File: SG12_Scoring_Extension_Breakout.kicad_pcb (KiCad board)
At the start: 2 copper layers, 100 x 100 mm, 41 parts, among them J1 RJ45, J10 Conn_01x02, J11 Conn_01x02, J12 Conn_01x02, J13 Conn_01x02, J14 Conn_01x02, J15 Conn_01x02, J16 Conn_02x04_Top_Bottom, J17 Conn_02x04_Top_Bottom, J18 Conn_02x04_Top_Bottom, J19 Conn_01x02, J2 Barrel_Jack_MountingPin, J3 Barrel_Jack_MountingPin, J4 Barrel_Jack_MountingPin, J5 Barrel_Jack_MountingPin, J6 Barrel_Jack_MountingPin, J7 Barrel_Jack_MountingPin, J8 Conn_02x08_Odd_Even, J9 Barrel_Jack_MountingPin, Q1 IRF4905, Q2 IRF4905, Q3 IRF4905, Q4 IRF4905, Q5 IRF4905, Q6 IRF4905

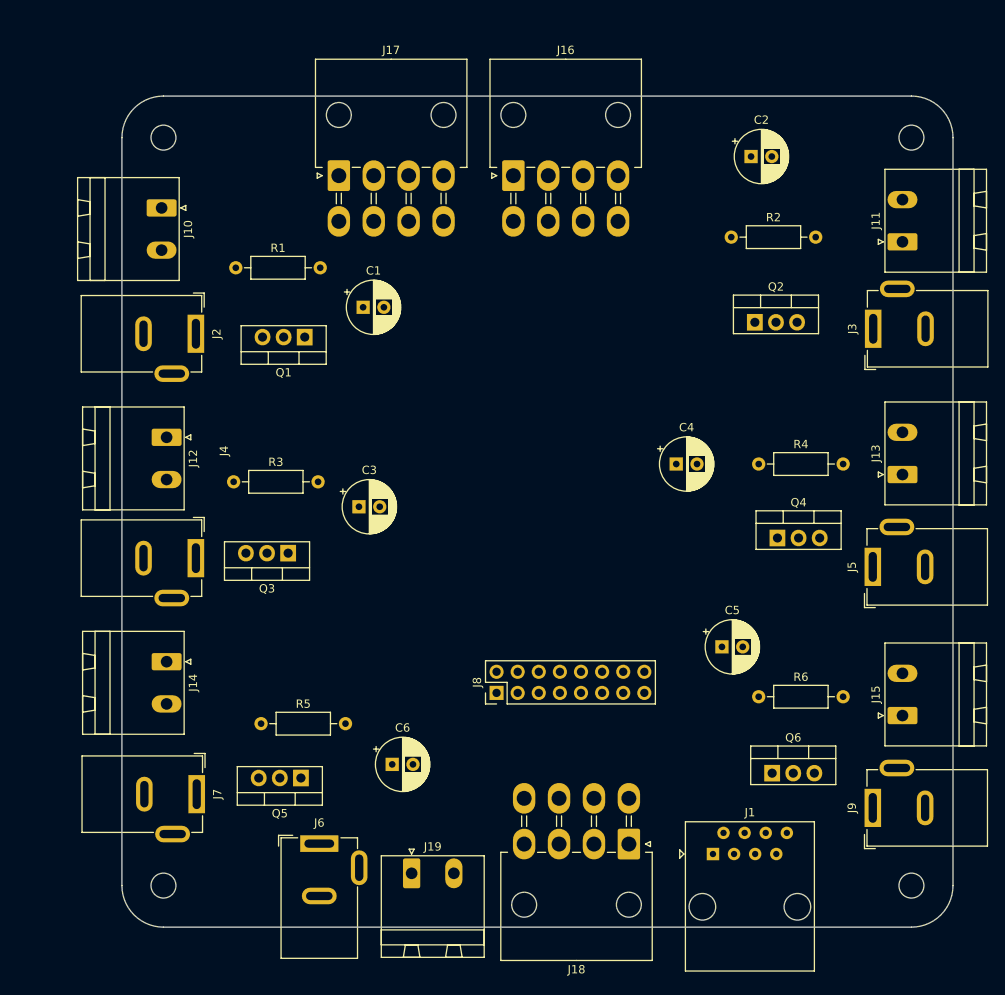
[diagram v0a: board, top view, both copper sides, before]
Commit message: Very nitpicky positioning on the Red and Green connectors
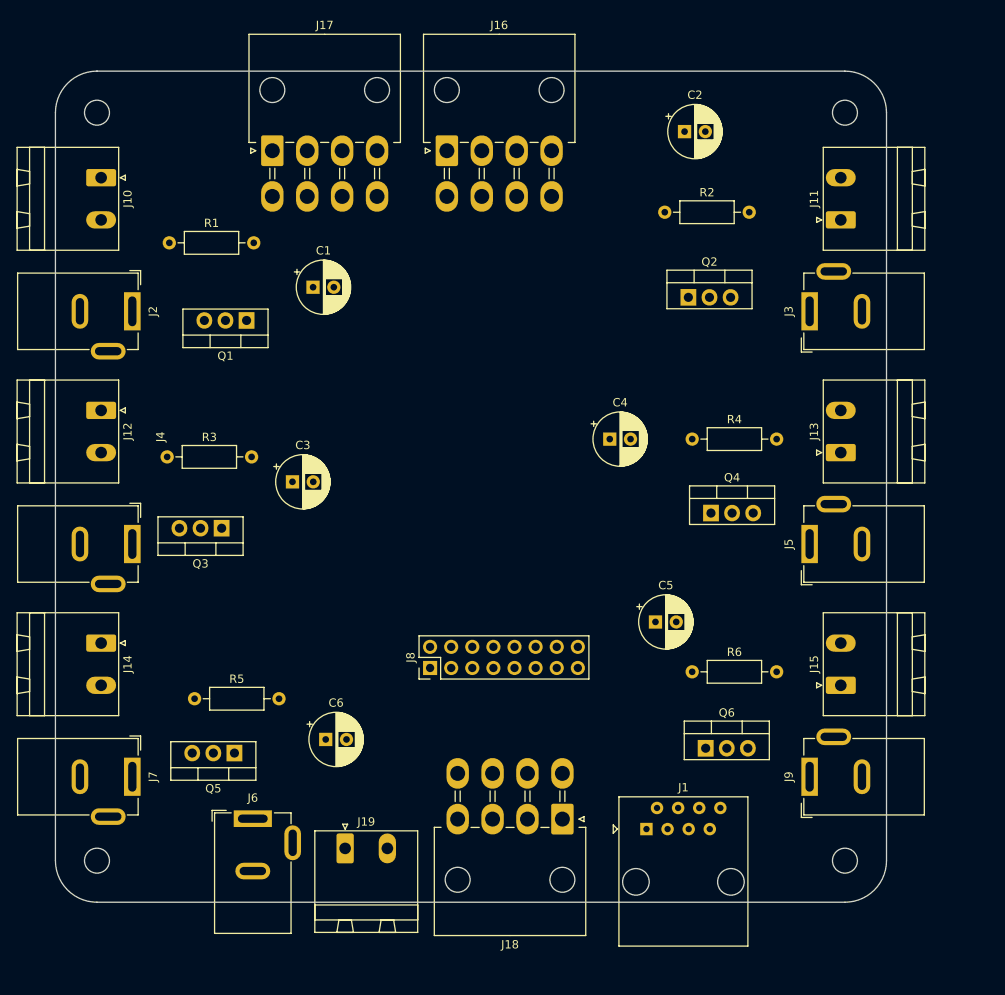
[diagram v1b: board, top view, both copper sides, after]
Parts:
- moved C3 8.54 mm to (123.5, 94.4)
- moved C6 8.54 mm to (127.5, 125.4)
- moved C2 8.54 mm to (170.7, 52.3)
- moved C4 8.54 mm to (161.7, 89.3)
- moved C5 8.54 mm to (167.2, 111.3)
- moved J1 8.54 mm to (166.1, 136.2)
- moved J16 8.54 mm to (142.1, 54.6)
- moved J17 8.54 mm to (121.1, 54.6)
- moved J18 8.54 mm to (156.0, 135.0)
- moved J19 8.54 mm to (129.9, 138.5)
- moved J6 8.54 mm to (118.8, 134.9)
- moved J8 8.54 mm to (140.1, 116.8)
- moved Q2 8.54 mm to (171.2, 72.2)
- moved Q3 8.54 mm to (115.0, 100.0)
- moved Q4 8.54 mm to (173.9, 98.2)
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
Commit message: Very nitpicky mofet and resistor placement
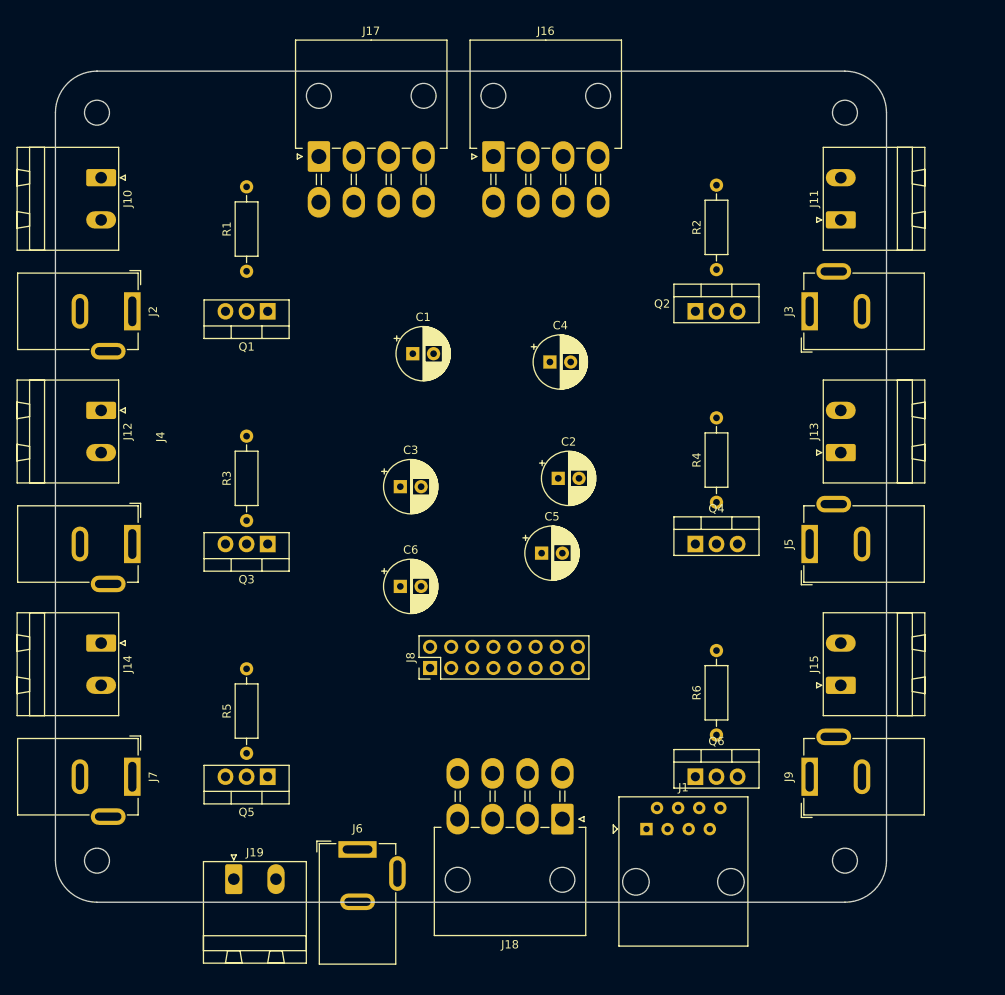
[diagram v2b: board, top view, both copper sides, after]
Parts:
- moved C2 44.4 mm to (155.5, 94.0)
- moved C6 20.5 mm to (136.5, 107.0)
- moved C5 16.0 mm to (153.5, 103.0)
- moved C1 14.4 mm to (138.0, 79.0)
- moved J19 13.9 mm to (116.5, 142.2)
- moved J6 13.1 mm to (131.3, 138.7)
- moved C3 13.0 mm to (136.5, 95.0)
- moved R3 12.3 mm to (118.0, 99.1), turned to 90 degrees
- moved C4 11.7 mm to (154.5, 80.0)
- moved R1 9.91 mm to (118.0, 69.1), turned to 90 degrees
- moved R2 9.29 mm to (174.5, 68.9), turned to 90 degrees
- moved R5 9.07 mm to (118.0, 127.1), turned to 90 degrees
- moved R4 8.15 mm to (174.5, 96.9), turned to 90 degrees
- moved R6 8.15 mm to (174.5, 124.9), turned to 90 degrees
- moved Q3 5.86 mm to (120.5, 101.9)
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
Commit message: Initial footprint placement
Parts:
- moved C6 44.8 mm to (179.5, 119.8), turned to 90 degrees
- moved C5 44.7 mm to (112.0, 119.6), turned to 90 degrees
- moved C2 38.6 mm to (179.5, 63.8), turned to 90 degrees
- moved C1 30.2 mm to (112.0, 63.6), turned to 90 degrees
- moved C4 27.6 mm to (179.5, 91.8), turned to 90 degrees
- moved C3 24.7 mm to (112.0, 91.6), turned to 90 degrees
- moved R3 4.92 mm to (118.0, 94.2)
- moved R5 4.92 mm to (118.0, 122.2)
- moved J19 4.24 mm to (113.5, 139.2)
- moved J8 4.01 mm to (136.5, 118.5)
- moved Q2 3.13 mm to (170.5, 71.2)
- moved Q4 3.13 mm to (170.5, 99.2)
- moved Q6 3.13 mm to (170.5, 127.2)
- moved R2 3.13 mm to (173.0, 66.2)
- moved R4 3.13 mm to (173.0, 94.2)
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
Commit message: Some initial routing
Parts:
- moved J8 7.27 mm to (136.1, 111.3)
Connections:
- J16 pad 6: /Red_PullUp -> /WhiteG_PullUp
- J16 pad 7: /WhiteG_PullUp -> /WhiteR_PullUp
- J16 pad 8: /WhiteR_PullUp -> /Red_PullUp
- J17 pad 6: /Red_PullUp -> /WhiteG_PullUp
- J17 pad 7: /WhiteG_PullUp -> /WhiteR_PullUp
- J17 pad 8: /WhiteR_PullUp -> /Red_PullUp
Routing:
- net /WhiteG_PullUp: track 0.00 -> 153.0 mm, vias 0 -> 1
- net /BlockingG_PullDown: track 0.00 -> 152.2 mm
- net /Green_PullDown: track 0.00 -> 135.4 mm, vias 0 -> 1
- net /WhiteR_PullUp: track 0.00 -> 134.4 mm, vias 0 -> 3
- net /Green_PullUp: track 0.00 -> 128.3 mm
- net /WhiteG_PullDown: track 0.00 -> 127.8 mm, vias 0 -> 1
- net /Red_PullUp: track 0.00 -> 124.7 mm, vias 0 -> 2
- net /Red_PullDown: track 0.00 -> 116.1 mm, vias 0 -> 1
- net /WhiteR_PullDown: track 0.00 -> 84.8 mm, vias 0 -> 1
- net /BlockingG_PullUp: track 0.00 -> 60.0 mm, vias 0 -> 1
- net /BlockingR_PullDown: track 0.00 -> 54.5 mm
- net /BlockingR_PullUp: track 0.00 -> 53.0 mm
- added copper zone on F.Cu, net /BlockingG_PullUp
- added copper zone on F.Cu, net /BlockingR_PullUp
- added copper zone on F.Cu, net /Green_PullUp
- added copper zone on F.Cu, net /Red_PullUp
- added copper zone on F.Cu, net /WhiteG_PullUp
- added copper zone on F.Cu, net /WhiteR_PullUp
- added copper zone on B.Cu, net GND

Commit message: Finished routing
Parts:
- moved J19 57.0 mm to (170.5, 139.2)
- moved J1 14.0 mm to (151.7, 134.9)
- moved J18 11.7 mm to (143.6, 134.7)
- moved J6 11.3 mm to (120.0, 135.7)
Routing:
- net /BlockingG_PullDown: track 152.2 -> 77.4 mm
- net +12V: track 0.00 -> 71.8 mm, vias 0 -> 2
- net GND: track 0.00 -> 70.2 mm
- net /WhiteG_PullDown: track 127.8 -> 75.6 mm, vias 1 -> 0
- net /Green_PullDown: track 135.4 -> 98.4 mm, vias 1 -> 0
- net /WhiteG_PullUp: track 153.0 -> 132.3 mm, vias 1 -> 2
- net /BlockingG_PullUp: track 60.0 -> 41.8 mm
- net /WhiteR_PullUp: track 134.4 -> 151.4 mm, vias 3 -> 2
- net /Green_PullUp: track 128.3 -> 112.0 mm, vias 0 -> 1
- net /BlockingR_PullUp: track 53.0 -> 38.2 mm
- net /Red_PullDown: track 116.1 -> 103.8 mm, vias 1 -> 2
- net /WhiteR_PullDown: track 84.8 -> 73.4 mm, vias 1 -> 2
- net /Red_PullUp: track 124.7 -> 116.6 mm, vias 2 -> 1
- net /BlockingR_PullDown: track 54.5 -> 57.5 mm
- added copper zone on B.Cu, net +12V
- added copper zone on F.Cu, net +12V
- added copper zone on B.Cu, net /BlockingG_PullUp
- added copper zone on B.Cu, net /Green_PullUp
- added copper zone on B.Cu, net /WhiteG_PullUp
- added copper zone on F.Cu, net GND
- removed copper zone on F.Cu, net /BlockingG_PullUp
- removed copper zone on F.Cu, net /Green_PullUp
- removed copper zone on F.Cu, net /WhiteG_PullUp

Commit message: Routing adjustments
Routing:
- net GND: track 70.2 -> 111.4 mm
- net /BlockingG_PullUp: track 41.8 -> 42.3 mm
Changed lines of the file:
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@@
   (segment (start 160.6075 133.63) (end 160.6075 132.36) (width 2) (layer "F.Cu") (net 1))
   (segment (start 159.3375 134.9) (end 160.6075 133.63) (width 2) (layer "F.Cu") (net 1))
+  (segment (start 173 132) (end 177 132) (width 4) (layer "F.Cu") (net 1))
   (segment (start 160.4375 129.2) (end 170.46 139.2225) (width 4) (layer "F.Cu") (net 1))
   (segment (start 151.365 117.235) (end 151.365 111.275) (width 2) (layer "F.Cu") (net 1))
@@
   (via (at 177 132) (size 4) (drill 1) (layers "F.Cu" "B.Cu") (net 1))
   (via (at 173 132) (size 4) (drill 1) (layers "F.Cu" "B.Cu") (net 1))
-  (segment (start 173 132) (end 177 132) (width 4) (layer "B.Cu") (net 1))
-  (segment (start 107.08 117.08) (end 107 117) (width 2) (layer "F.Cu") (net 2))
-  (segment (start 112 61.08) (end 107.08 61.08) (width 2) (layer "F.Cu") (net 2))
-  (segment (start 107.08 89.08) (end 107 89) (width 2) (layer "F.Cu") (net 2))
+  (segment (start 102.32 117.08) (end 100.5 118.9) (width 1.5) (layer "F.Cu") (net 2))
+  (segment (start 102.32 89.08) (end 100.5 90.9) (width 1.5) (layer "F.Cu") (net 2))
+  (segment (start 112 61.08) (end 102.32 61.08) (width 1.5) (layer "F.Cu") (net 2))
+  (segment (start 112 89.08) (end 102.32 89.08) (width 1.5) (layer "F.Cu") (net 2))
   (segment (start 151.365 108.735) (end 153.905 108.735) (width 1.5) (layer "F.Cu") (net 2))
   (segment (start 153.905 108.735) (end 177.735 108.735) (width 1.5) (layer "F.Cu") (net 2))
-  (segment (start 112 117.08) (end 107.08 117.08) (width 2) (layer "F.Cu") (net 2))
   (segment (start 177.735 108.735) (end 182.82 113.82) (width 1.5) (layer "F.Cu") (net 2))
+  (segment (start 112 117.08) (end 102.32 117.08) (width 1.5) (layer "F.Cu") (net 2))
   (segment (start 182.82 113.82) (end 189.5 113.82) (width 1.5) (layer "F.Cu") (net 2))
-  (segment (start 112 89.08) (end 107.08 89.08) (width 2) (layer "F.Cu") (net 2))
-  (segment (start 183.72 61.28) (end 184 61) (width 2) (layer "B.Cu") (net 2))
-  (segment (start 179.46 89.28) (end 183.72 89.28) (width 2) (layer "B.Cu") (net 2))
-  (segment (start 179.46 61.28) (end 183.72 61.28) (width 2) (layer "B.Cu") (net 2))
-  (segment (start 183.72 89.28) (end 184 89) (width 2) (layer "B.Cu") (net 2))
-  (segment (start 184.72 117.28) (end 185 117) (width 2) (layer "B.Cu") (net 2))
-  (segment (start 179.46 117.28) (end 184.72 117.28) (width 2) (layer "B.Cu") (net 2))
+  (segment (start 102.32 61.08) (end 100.5 62.9) (width 1.5) (layer "F.Cu") (net 2))
+  (segment (start 179.46 61.28) (end 186.04 61.28) (width 1.5) (layer "B.Cu") (net 2))
+  (segment (start 186.04 61.28) (end 189.5 57.82) (width 1.5) (layer "B.Cu") (net 2))
+  (segment (start 179.46 117.28) (end 186.04 117.28) (width 1.5) (layer "B.Cu") (net 2))
+  (segment (start 186.04 89.28) (end 189.5 85.82) (width 1.5) (layer "B.Cu") (net 2))
+  (segment (start 179.46 89.28) (end 186.04 89.28) (width 1.5) (layer "B.Cu") (net 2))
+  (segment (start 186.04 117.28) (end 189.5 113.82) (width 1.5) (layer "B.Cu") (net 2))
   (segment (start 120.54 58.54) (end 118 56) (width 0.25) (layer "F.Cu") (net 3))
   (segment (start 136.125 111.275) (end 127 102.15) (width 0.25) (layer "F.Cu") (net 3))
@@
   (segment (start 159.1 72) (end 138.060303 72) (width 4) (layer "B.Cu") (net 12))
   (segment (start 138.060303 72) (end 135.1 69.039697) (width 4) (layer "B.Cu") (net 12))
-  (segment (start 147.46 111.760054) (end 141.220054 118) (width 0.25) (layer "F.Cu") (net 13))
   (segment (start 146.285 108.735) (end 147.46 109.91) (width 0.25) (layer "F.Cu") (net 13))
-  (segment (start 147.46 109.91) (end 147.46 111.760054) (width 0.25) (layer "F.Cu") (net 13))
-  (segment (start 141.220054 118) (end 141 118) (width 0.25) (layer "F.Cu") (net 13))
+  (segment (start 147.46 112.650027) (end 142.110027 118) (width 0.25) (layer "F.Cu") (net 13))
+  (segment (start 142.110027 118) (end 141 118) (width 0.25) (layer "F.Cu") (net 13))
+  (segment (start 147.46 109.91) (end 147.46 112.650027) (width 0.25) (layer "F.Cu") (net 13))
   (via (at 141 118) (size 0.8) (drill 0.4) (layers "F.Cu" "B.Cu") (net 13))
   (segment (start 119.155 123.285) (end 115.46 126.98) (width 0.25) (layer "B.Cu") (net 13))

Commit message: Silkscreen Labels
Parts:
- renumbered J7 to BlockG1, J14 to BlockG2, J9 to BlockR1, J15 to BlockR2, C3 to C1, C1 to C3, J2 to Green1, J10 to Green2, J8 to J1, J16 to J2, J17 to J3, J18 to PWR1, J19 to PWR2, J6 to PWR3, J3 to Red1, J11 to Red2, J1 to SIG1, J4 to WhiteG1, J12 to WhiteG2, J5 to WhiteR1, J13 to WhiteR2
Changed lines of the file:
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@@
     (property "ki_keywords" "Single P-Channel HEXFET Power MOSFET")
     (attr through_hole)
-    (fp_text reference "Q4" (at 7 -3.9) (layer "F.SilkS")
+    (fp_text reference "Q4" (at 8.54 -1.18 90) (layer "F.SilkS")
         (effects (font (size 1 1) (thickness 0.15)))
     )
@@
     (property "ki_keywords" "connector")
     (attr through_hole)
-    (fp_text reference "J17" (at 6.3 -15.1) (layer "F.SilkS")
+    (fp_text reference "J3" (at 6.3 8.725) (layer "F.SilkS")
         (effects (font (size 1 1) (thickness 0.15)))
     )
@@
     (property "ki_keywords" "DC power barrel jack connector")
     (attr through_hole)
-    (fp_text reference "J2" (at 0 -2.5 90) (layer "F.SilkS")
+    (fp_text reference "Green1" (at 0 -2.75 90) (layer "F.SilkS")
         (effects (font (size 1 1) (thickness 0.15)))
     )
@@
     (property "ki_keywords" "connector")
     (attr through_hole)
-    (fp_text reference "J10" (at 2.54 -3.2 90) (layer "F.SilkS")
+    (fp_text reference "Green2" (at 2.54 -3.5 90) (layer "F.SilkS")
         (effects (font (size 1 1) (thickness 0.15)))
     )
@@
     (property "ki_keywords" "connector")
     (attr through_hole)
-    (fp_text reference "J19" (at 2.54 -3.2) (layer "F.SilkS")
+    (fp_text reference "PWR2" (at 2.54 -3.2) (layer "F.SilkS")
         (effects (font (size 1 1) (thickness 0.15)))
     )
@@
     (property "ki_keywords" "connector")
     (attr through_hole)
-    (fp_text reference "J16" (at 6.3 -15.1) (layer "F.SilkS")
+    (fp_text reference "J2" (at 6.3 8.725) (layer "F.SilkS")
         (effects (font (size 1 1) (thickness 0.15)))
     )
@@
     (property "ki_keywords" "Single P-Channel HEXFET Power MOSFET")
     (attr through_hole)
-    (fp_text reference "Q6" (at 7 -4.27) (layer "F.SilkS")
+    (fp_text reference "Q6" (at 8.54 -1.18 90) (layer "F.SilkS")
         (effects (font (size 1 1) (thickness 0.15)))
     )
@@
     (property "ki_keywords" "Single P-Channel HEXFET Power MOSFET")
     (attr through_hole)
-    (fp_text reference "Q3" (at -5.46 -0.1) (layer "F.SilkS")
+    (fp_text reference "Q3" (at -3.46 -1.02 90) (layer "F.SilkS")
         (effects (font (size 1 1) (thickness 0.15)))
     )
@@
     (property "ki_keywords" "DC power barrel jack connector")
     (attr through_hole)
-    (fp_text reference "J3" (at 0 -1.96 90) (layer "F.SilkS")
+    (fp_text reference "Red1" (at 0 -2.75 90) (layer "F.SilkS")
         (effects (font (size 1 1) (thickness 0.15)))
     )
@@
     (property "ki_keywords" "connector")
     (attr through_hole)
-    (fp_text reference "J12" (at 2.54 -3.2 90) (layer "F.SilkS")
+    (fp_text reference "WhiteG2" (at 2.54 -4.5 90) (layer "F.SilkS")
         (effects (font (size 1 1) (thickness 0.15)))
     )
@@
     (property "ki_keywords" "connector")
     (attr through_hole)
-    (fp_text reference "J14" (at 2.54 -3.2 90) (layer "F.SilkS")
+    (fp_text reference "BlockG2" (at 2.54 -4.5 90) (layer "F.SilkS")
         (effects (font (size 1 1) (thickness 0.15)))
     )
@@
     (property "ki_keywords" "connector")
     (attr through_hole)
-    (fp_text reference "J13" (at 2.54 -3.2 90) (layer "F.SilkS")
+    (fp_text reference "WhiteR2" (at 2.54 -4.5 90) (layer "F.SilkS")
         (effects (font (size 1 1) (thickness 0.15)))
     )
@@
     (property "ki_keywords" "Single P-Channel HEXFET Power MOSFET")
     (attr through_hole)
-    (fp_text reference "Q1" (at -5.46 -0.1) (layer "F.SilkS")
+    (fp_text reference "Q1" (at -3.46 -1.02 90) (layer "F.SilkS")
         (effects (font (size 1 1) (thickness 0.15)))
     )
@@
     (property "ki_keywords" "cap capacitor")
     (attr through_hole)
-    (fp_text reference "C3" (at 6.5 0 90) (layer "F.SilkS")
+    (fp_text reference "C1" (at 6.5 0 90) (layer "F.SilkS")
         (effects (font (size 1 1) (thickness 0.15)))
     )
@@
     (property "ki_keywords" "DC power barrel jack connector")
     (attr through_hole)
-    (fp_text reference "J5" (at 0 -1.96 90) (layer "F.SilkS")
+    (fp_text reference "WhiteR1" (at 0 -2.75 90) (layer "F.SilkS")
         (effects (font (size 1 1) (thickness 0.15)))
     )
@@
     (property "ki_keywords" "Single P-Channel HEXFET Power MOSFET")
     (attr through_hole)
-    (fp_text reference "Q2" (at 7 -3.9) (layer "F.SilkS")
+    (fp_text reference "Q2" (at 8.54 -1.18 90) (layer "F.SilkS")
         (effects (font (size 1 1) (thickness 0.15)))
     )
@@
     (property "ki_keywords" "Single P-Channel HEXFET Power MOSFET")
     (attr through_hole)
-    (fp_text reference "Q5" (at 2.54 -4.27) (layer "F.SilkS")
+    (fp_text reference "Q5" (at -3.46 -1.02 90) (layer "F.SilkS")
         (effects (font (size 1 1) (thickness 0.15)))
     )
@@
     (property "ki_keywords" "connector")
     (attr through_hole)
-    (fp_text reference "J15" (at 2.54 -3.2 90) (layer "F.SilkS")
+    (fp_text reference "BlockR2" (at 2.54 -4.5 90) (layer "F.SilkS")
         (effects (font (size 1 1) (thickness 0.15)))
     )
@@
     (property "ki_keywords" "connector")
     (attr through_hole)
-    (fp_text reference "J8" (at 1.27 -2.33 90) (layer "F.SilkS")
+    (fp_text reference "J1" (at 1.27 -2.33 90) (layer "F.SilkS")
         (effects (font (size 1 1) (thickness 0.15)))
     )
@@
     (property "ki_keywords" "connector")
     (attr through_hole)
-    (fp_text reference "J11" (at 2.54 -3.2 90) (layer "F.SilkS")
+    (fp_text reference "Red2" (at 2.54 -4.5 90) (layer "F.SilkS")
         (effects (font (size 1 1) (thickness 0.15)))
     )
@@
     (property "ki_keywords" "connector")
     (attr through_hole)
-    (fp_text reference "J18" (at 6.3 -15.1) (layer "F.SilkS")
+    (fp_text reference "PWR1" (at 6.3 8.7) (layer "F.SilkS")
         (effects (font (size 1 1) (thickness 0.15)))
     )
@@
     (property "ki_keywords" "DC power barrel jack connector")
     (attr through_hole)
-    (fp_text reference "J7" (at 0 -2.5 90) (layer "F.SilkS")
+    (fp_text reference "BlockG1" (at 0 -2.75 90) (layer "F.SilkS")
         (effects (font (size 1 1) (thickness 0.15)))
     )
@@
     (property "ki_keywords" "DC power barrel jack connector")
     (attr through_hole)
-    (fp_text reference "J6" (at 0 -2.5) (layer "F.SilkS")
+    (fp_text reference "PWR3" (at 0 -2.5) (layer "F.SilkS")
         (effects (font (size 1 1) (thickness 0.15)))
     )
@@
     (property "ki_keywords" "cap capacitor")
     (attr through_hole)
-    (fp_text reference "C1" (at 6.5 0 90) (layer "F.SilkS")
+    (fp_text reference "C3" (at 6.5 0 90) (layer "F.SilkS")
         (effects (font (size 1 1) (thickness 0.15)))
     )
@@
     (property "ki_keywords" "DC power barrel jack connector")
     (attr through_hole)
-    (fp_text reference "J4" (at -12.9 -3.4 90) (layer "F.SilkS")
+    (fp_text reference "WhiteG1" (at 0.1 -2.75 90) (layer "F.SilkS")
         (effects (font (size 1 1) (thickness 0.15)))
     )
@@
     (property "ki_keywords" "8P8C RJ socket connector")
     (attr through_hole)
-    (fp_text reference "J1" (at 4.445 -5) (layer "F.SilkS")
+    (fp_text reference "SIG1" (at 4.445 -5) (layer "F.SilkS")
         (effects (font (size 1 1) (thickness 0.15)))
     )
@@
     (property "ki_keywords" "DC power barrel jack connector")
     (attr through_hole)
-    (fp_text reference "J9" (at 0 -1.96 90) (layer "F.SilkS")
+    (fp_text reference "BlockR1" (at 0 -2.75 90) (layer "F.SilkS")
         (effects (font (size 1 1) (thickness 0.15)))
     )
